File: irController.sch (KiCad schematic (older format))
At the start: 26 parts, among them P1 ZX62R-B-5P, P2 GPIO_USER, P3 WRITE_PROG, Q1 Q_NMOS, SW1 SKRPACE010, SW2 SKRPACE010, U1 NJM2845, U2 ESP-13-WROOM-02, U3 IRSNS_GP1UXC41QS

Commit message: バックアップファイル等削除し整理
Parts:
- C1, C2, C3, C4: symbol C -> irController-rescue:C
- D1, D2, D3: symbol LED-RESCUE-irController -> irController-rescue:LED-RESCUE-irController
- P1: symbol USB_OTG-RESCUE-irController -> irController-rescue:USB_OTG-RESCUE-irController
- P2: symbol CONN_01X02 -> irController-rescue:CONN_01X02
- P3: symbol CONN_01X03 -> irController-rescue:CONN_01X03
- Q1: symbol Q_NMOS_GSD -> irController-rescue:Q_NMOS_GSD
- R1, R10, R2, R3, R4, R5, R6, R7, R8, R9: symbol R -> irController-rescue:R
- SW1, SW2: symbol Switch_DPST -> irController-rescue:Switch_DPST
- U1: symbol NJM2845 -> irController-rescue:NJM2845
- U2: symbol ESP-13-WROOM-02 -> irController-rescue:ESP-13-WROOM-02
- U3: symbol IRSNS_GP1UXC41QS -> irController-rescue:IRSNS_GP1UXC41QS

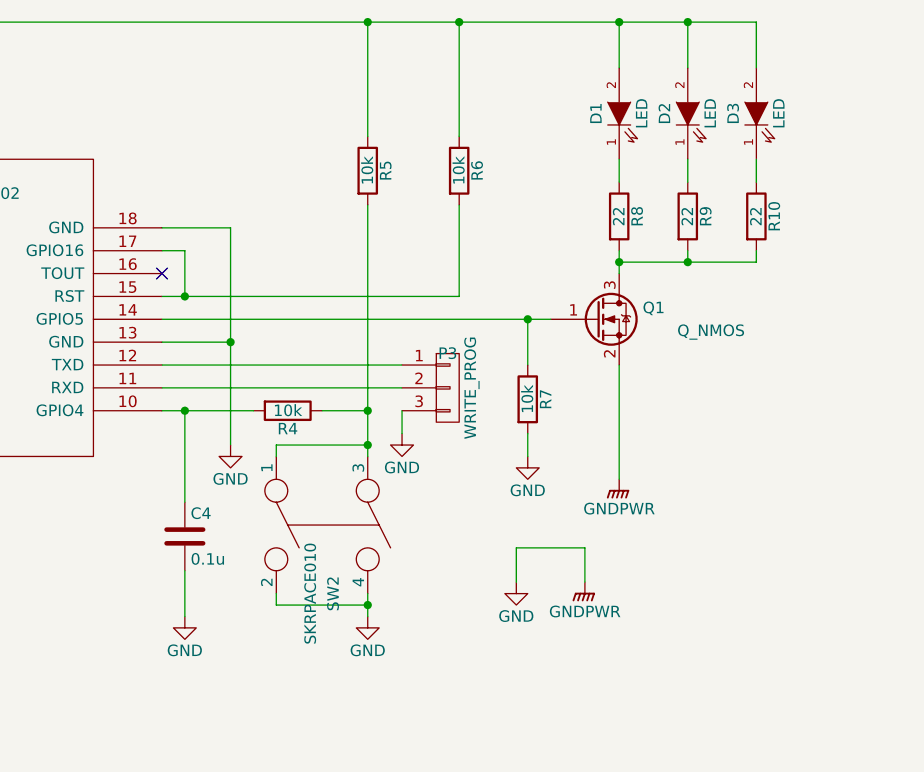
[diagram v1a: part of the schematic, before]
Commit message: コネクタ変更
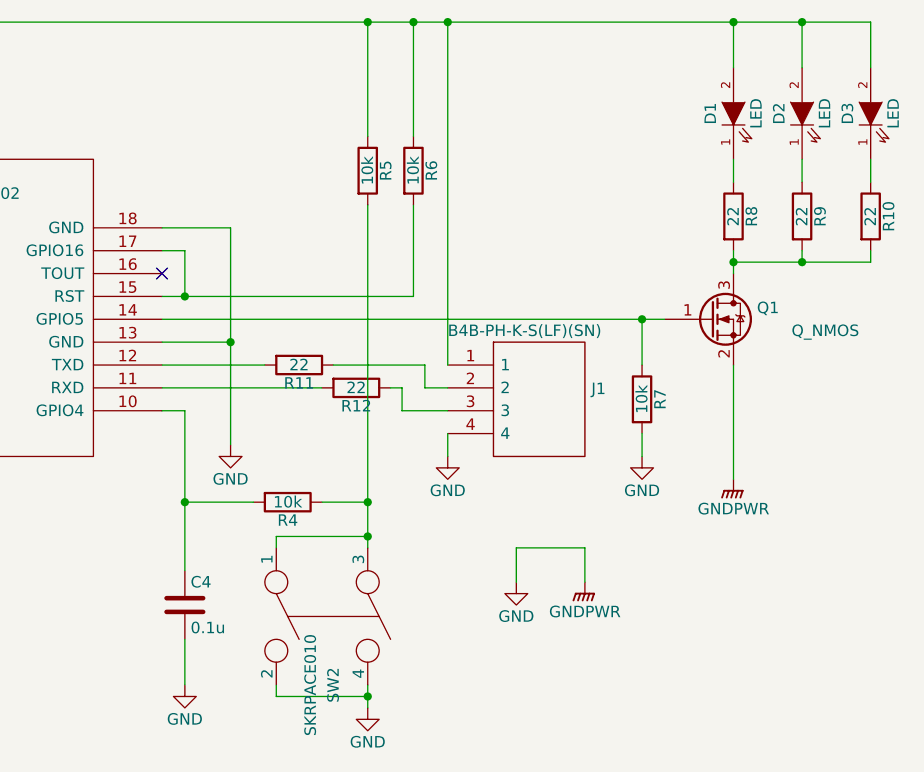
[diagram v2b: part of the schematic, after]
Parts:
- removed P3: WRITE_PROG, Socket_Strips:Socket_Strip_Straight_1x03, symbol irController-rescue:CONN_01X03
- added J1: B4B-PH-K-S(LF)(SN), SamacSys:SHDR4W60P0X200_1X4_990X450X600P, symbol SamacSys:B4B-PH-K-S(LF)(SN)
- added R11, R12: 22, Resistors_SMD:R_0603, symbol irController-rescue:R
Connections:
- net GND: now also J1.4
- net at C2.1, C3.1, D1.2 (A)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: now also J1.1
- net at U2.11 (RXD): now also R12.2
- net at U2.12 (TXD): now also R11.2
- new net: J1.2, R11.1
- new net: J1.3, R12.1
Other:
- moved on the sheet: C4, D1, D2, D3, Q1, R10, R4, R6, R7, R8, R9, SW2

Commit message: 一旦完成
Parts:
- R1, R10, R11, R12, R2, R3, R4, R5, R6, R7, R8, R9: footprint Resistors_SMD:R_0603 -> Resistor_SMD:R_0603_1608Metric
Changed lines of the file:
@@
 F 0 "R8" V 9480 3150 50  0000 C CNN
 F 1 "22" V 9400 3150 50  0000 C CNN
-F 2 "Resistors_SMD:R_0603" V 9330 3150 50  0001 C CNN
+F 2 "Resistor_SMD:R_0603_1608Metric" V 9330 3150 50  0001 C CNN
 F 3 "" H 9400 3150 50  0000 C CNN
 	1    9400 3150
@@
 F 0 "R9" V 9780 3150 50  0000 C CNN
 F 1 "22" V 9700 3150 50  0000 C CNN
-F 2 "Resistors_SMD:R_0603" V 9630 3150 50  0001 C CNN
+F 2 "Resistor_SMD:R_0603_1608Metric" V 9630 3150 50  0001 C CNN
 F 3 "" H 9700 3150 50  0000 C CNN
 	1    9700 3150
@@
 F 0 "R10" V 10080 3150 50  0000 C CNN
 F 1 "22" V 10000 3150 50  0000 C CNN
-F 2 "Resistors_SMD:R_0603" V 9930 3150 50  0001 C CNN
+F 2 "Resistor_SMD:R_0603_1608Metric" V 9930 3150 50  0001 C CNN
 F 3 "" H 10000 3150 50  0000 C CNN
 	1    10000 3150
@@
 F 0 "R2" V 3730 3500 50  0000 C CNN
 F 1 "10k" V 3650 3500 50  0000 C CNN
-F 2 "Resistors_SMD:R_0603" V 3580 3500 50  0001 C CNN
+F 2 "Resistor_SMD:R_0603_1608Metric" V 3580 3500 50  0001 C CNN
 F 3 "" H 3650 3500 50  0000 C CNN
 	1    3650 3500
@@
 F 0 "R3" V 4480 4150 50  0000 C CNN
 F 1 "10k" V 4400 4150 50  0000 C CNN
-F 2 "Resistors_SMD:R_0603" V 4330 4150 50  0001 C CNN
+F 2 "Resistor_SMD:R_0603_1608Metric" V 4330 4150 50  0001 C CNN
 F 3 "" H 4400 4150 50  0000 C CNN
 	1    4400 4150
@@
 F 0 "R6" V 8080 2950 50  0000 C CNN
 F 1 "10k" V 8000 2950 50  0000 C CNN
-F 2 "Resistors_SMD:R_0603" V 7930 2950 50  0001 C CNN
+F 2 "Resistor_SMD:R_0603_1608Metric" V 7930 2950 50  0001 C CNN
 F 3 "" H 8000 2950 50  0000 C CNN
 	1    8000 2950
@@
 F 0 "R1" V 3430 3500 50  0000 C CNN
 F 1 "10k" V 3350 3500 50  0000 C CNN
-F 2 "Resistors_SMD:R_0603" V 3280 3500 50  0001 C CNN
+F 2 "Resistor_SMD:R_0603_1608Metric" V 3280 3500 50  0001 C CNN
 F 3 "" H 3350 3500 50  0000 C CNN
 	1    3350 3500
@@
 $EndComp
 $Comp
-L irController-rescue:ESP-13-WROOM-02 U2
-U 1 1 585A8532
-P 5950 3500
-F 0 "U2" H 5950 3400 50  0000 C CNN
-F 1 "ESP-13-WROOM-02" H 5950 3950 50  0000 C CNN
-F 2 "ESP-WROOM-02:ESP-13-WROOM-02" H 5850 3500 50  0001 C CNN
-F 3 "" H 5850 3500 50  0001 C CNN
-	1    5950 3500
-	1    0    0    -1
-$EndComp
-$Comp
 L irController-rescue:R R5
 U 1 1 585D6283
@@
 F 0 "R5" V 7880 2950 50  0000 C CNN
 F 1 "10k" V 7800 2950 50  0000 C CNN
-F 2 "Resistors_SMD:R_0603" V 7730 2950 50  0001 C CNN
+F 2 "Resistor_SMD:R_0603_1608Metric" V 7730 2950 50  0001 C CNN
 F 3 "" H 7800 2950 50  0000 C CNN
 	1    7800 2950
@@
 F 0 "R4" V 7530 4400 50  0000 C CNN
 F 1 "10k" V 7450 4400 50  0000 C CNN
-F 2 "Resistors_SMD:R_0603" V 7380 4400 50  0001 C CNN
+F 2 "Resistor_SMD:R_0603_1608Metric" V 7380 4400 50  0001 C CNN
 F 3 "" H 7450 4400 50  0000 C CNN
 	1    7450 4400
@@
 F 0 "R7" V 9080 3950 50  0000 C CNN
 F 1 "10k" V 9000 3950 50  0000 C CNN
-F 2 "Resistors_SMD:R_0603" V 8930 3950 50  0001 C CNN
+F 2 "Resistor_SMD:R_0603_1608Metric" V 8930 3950 50  0001 C CNN
 F 3 "" H 9000 3950 50  0000 C CNN
 	1    9000 3950
@@
 F 0 "R11" V 7580 3800 50  0000 C CNN
 F 1 "22" V 7500 3800 50  0000 C CNN
-F 2 "Resistors_SMD:R_0603" V 7430 3800 50  0001 C CNN
+F 2 "Resistor_SMD:R_0603_1608Metric" V 7430 3800 50  0001 C CNN
 F 3 "" H 7500 3800 50  0000 C CNN
 	1    7500 3800
@@
 F 0 "R12" V 7830 3900 50  0000 C CNN
 F 1 "22" V 7750 3900 50  0000 C CNN
-F 2 "Resistors_SMD:R_0603" V 7680 3900 50  0001 C CNN
+F 2 "Resistor_SMD:R_0603_1608Metric" V 7680 3900 50  0001 C CNN
 F 3 "" H 7750 3900 50  0000 C CNN
 	1    7750 3900
@@
 Wire Wire Line
 	7000 4400 7000 4700
+$Comp
+L irController-rescue:ESP-13-WROOM-02 U2
+U 1 1 585A8532
+P 5950 3500
+F 0 "U2" H 5950 3400 50  0000 C CNN
+F 1 "ESP-13-WROOM-02" H 5950 3950 50  0000 C CNN
+F 2 "ESP-WROOM-02:ESP-13-WROOM-02" H 5850 3500 50  0001 C CNN
+F 3 "" H 5850 3500 50  0001 C CNN
+	1    5950 3500
+	1    0    0    -1
+$EndComp
 $EndSCHEMATC

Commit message: 発注時データ
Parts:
- added R13: 22, Resistor_SMD:R_0603_1608Metric, symbol irController-rescue:R
- P1: footprint OriginalLibConn:USB_MICRO_HRS_ZX62R-B-5P -> Connector_USB:USB_Micro-B_Wuerth_629105150521
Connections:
- net at R1.2, SW1.1, SW1.3: now also R13.2; no longer U2.8 (GPIO0)
- new net: R13.1, U2.8 (GPIO0)
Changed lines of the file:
@@
 F 0 "P1" H 1575 3275 50  0000 C CNN
 F 1 "ZX62R-B-5P" H 1250 3600 50  0000 C CNN
-F 2 "OriginalLibConn:USB_MICRO_HRS_ZX62R-B-5P" V 1200 3300 50  0001 C CNN
+F 2 "Connector_USB:USB_Micro-B_Wuerth_629105150521" V 1200 3300 50  0001 C CNN
 F 3 "" V 1200 3300 50  0000 C CNN
 	1    1250 3400
@@
 	3350 3650 3350 3900
 Wire Wire Line
-	4950 3900 3350 3900
+	4950 3900 4050 3900
 Connection ~ 3350 3900
 Wire Wire Line
@@
 	1    0    0    -1
 $EndComp
+$Comp
+L irController-rescue:R R13
+U 1 1 5E13DBE1
+P 3900 3900
+F 0 "R13" V 3980 3900 50  0000 C CNN
+F 1 "22" V 3900 3900 50  0000 C CNN
+F 2 "Resistor_SMD:R_0603_1608Metric" V 3830 3900 50  0001 C CNN
+F 3 "" H 3900 3900 50  0000 C CNN
+	1    3900 3900
+	0    1    1    0
+$EndComp
+Wire Wire Line
+	3750 3900 3350 3900
 $EndSCHEMATC
